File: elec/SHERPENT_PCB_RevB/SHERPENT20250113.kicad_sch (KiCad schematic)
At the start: 111 parts, among them J1 2137160001, J2 Conn_01x03_Socket, J3 Conn_01x03_Socket, J4 Conn_01x03_Socket, Q1 PMOS, Q2 Q_NMOS_GSD, Q3 Q_NMOS_GSD, Q5 PMOS, Q6 PMOS, SW1 CT1102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

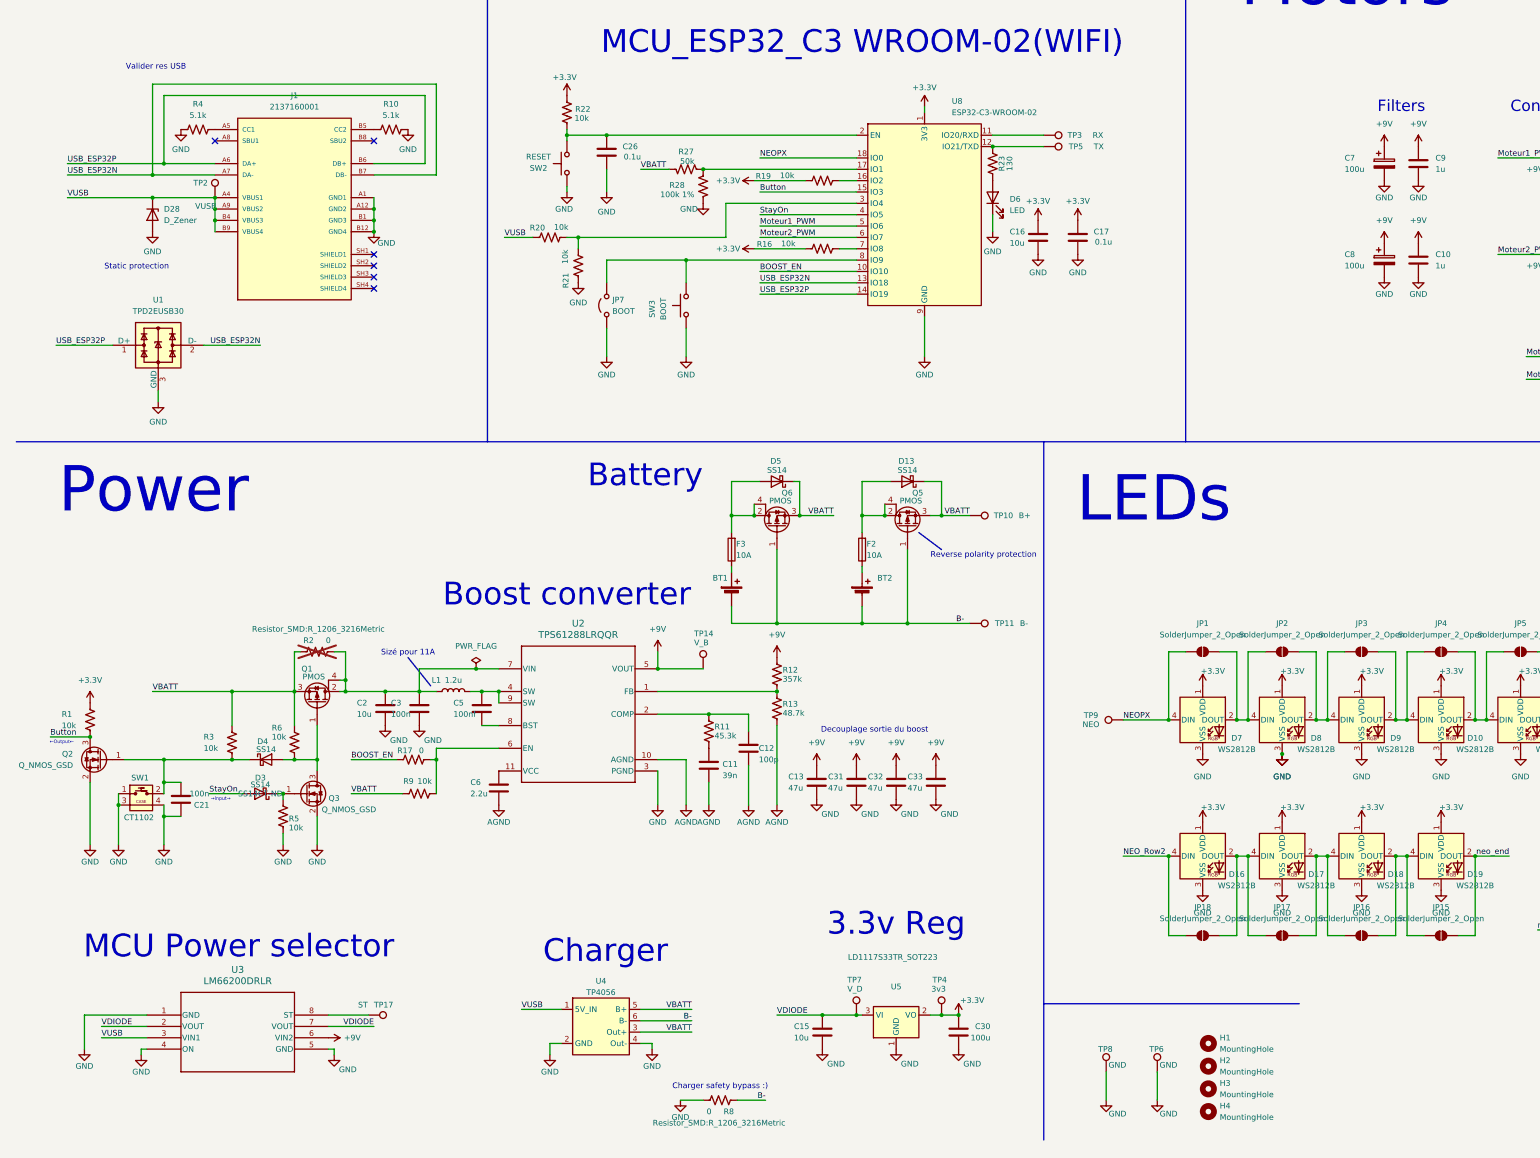
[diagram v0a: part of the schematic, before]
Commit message: ajouté les part numbers dans revB
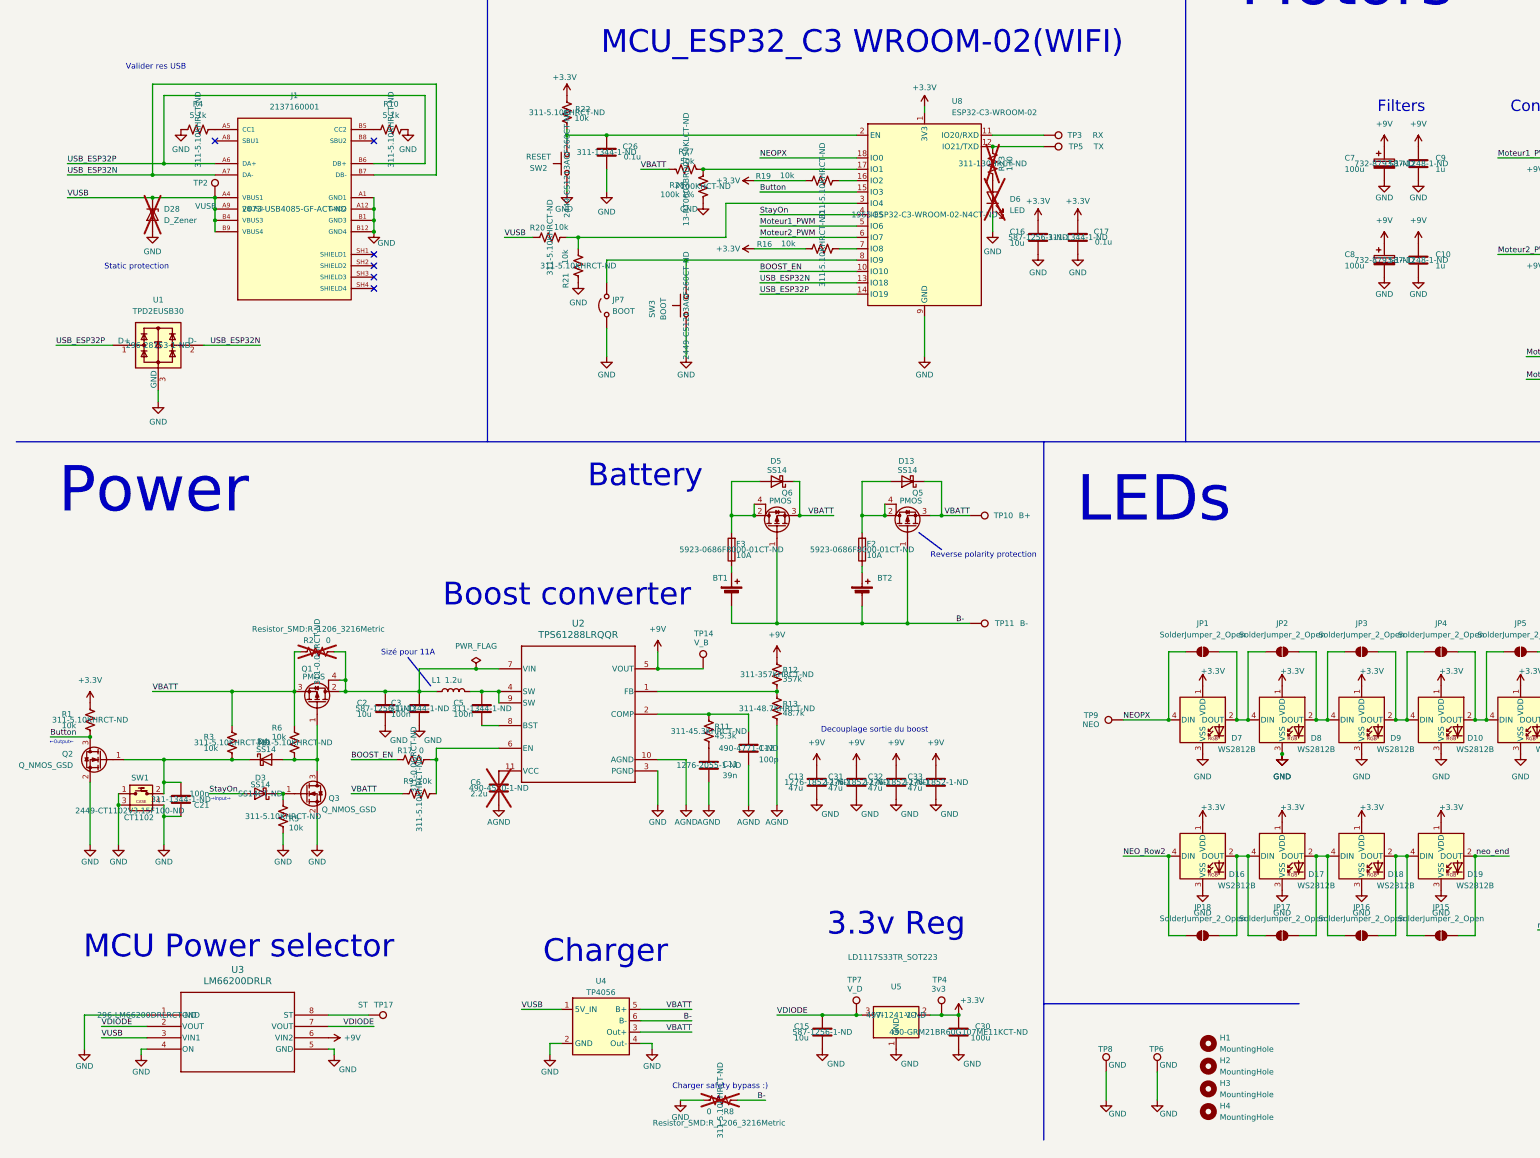
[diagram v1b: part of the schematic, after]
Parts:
- C10, C9: DigiKey (none) -> 587-1248-1-ND
- C11: DigiKey (none) -> 1276-2055-1-ND
- C12: DigiKey (none) -> 490-4771-1-ND
- C13, C31, C32, C33: DigiKey (none) -> 1276-1852-1-ND
- C15, C16, C2: DigiKey (none) -> 587-1256-1-ND
- C17, C21, C26, C3: DigiKey (none) -> 311-1344-1-ND
- C30: DigiKey (none) -> 490-GRM21BR60G107ME11KCT-ND
- C5: value 100nf -> 100n; DigiKey (none) -> 311-1344-1-ND
- C6: DigiKey (none) -> 490-4520-1-ND; now not fitted
- C7, C8: DigiKey (none) -> 732-8793-1-ND
- D28, D6: now not fitted
- F2, F3: DigiKey (none) -> 5923-0686F8000-01CT-ND
- J1: DigiKey (none) -> 2073-USB4085-GF-ACT-ND
- R1, R10, R16, R19, R20, R21, R22, R3, R4, R5, R6, R9: DigiKey (none) -> 311-5.10KHRCT-ND
- R11: DigiKey (none) -> 311-45.3KHRCT-ND
- R12: DigiKey (none) -> 311-357KHRCT-ND
- R13: DigiKey (none) -> 311-48.7KHRCT-ND
- R17, R2: DigiKey (none) -> 311-0.0GRCT-ND
- R23: DigiKey (none) -> 311-130HRCT-ND; now not fitted
- R27: DigiKey (none) -> 13-RT0603BRD0750KLCT-ND
- R28: DigiKey (none) -> P100KHCT-ND
- R8: DigiKey (none) -> 311-5.10KHRCT-ND; now not fitted
- SW1: DigiKey (none) -> 2449-CT1102V3.15F100-ND
- SW2, SW3: DigiKey (none) -> 2449-CS1213AGF260CT-ND
- U1: DigiKey (none) -> 296-28153-1-ND
- U3: DigiKey (none) -> 296-LM66200DRLRCT-ND
- U5: DigiKey (none) -> 497-1241-1-ND
- U8: DigiKey (none) -> 1965-ESP32-C3-WROOM-02-N4CT-ND

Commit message: Correction d'erreur sur le schéma
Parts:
- C6: now fitted
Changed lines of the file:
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@@
 		(in_bom yes)
 		(on_board yes)
-		(dnp yes)
+		(dnp no)
 		(property "Reference" "C6"
 			(at 114.3 203.2 0)
